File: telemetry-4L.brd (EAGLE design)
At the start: 69.8 x 22.9 mm, 64 parts, among them SW1 MF-SW-TACT-4.2MM, SW2 PCM12SMTR, U1 ATSAMD21G18A-MUT, U2 SPX3819M5-L-3-0, U3 MCP73831T-2ACI/OT, U4 IRLML6344TRPBF, U5 SIM868, U6 BMP280, U7 MPU-9250, X1 S2B-PH-SM4-TB(LF)(SN)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

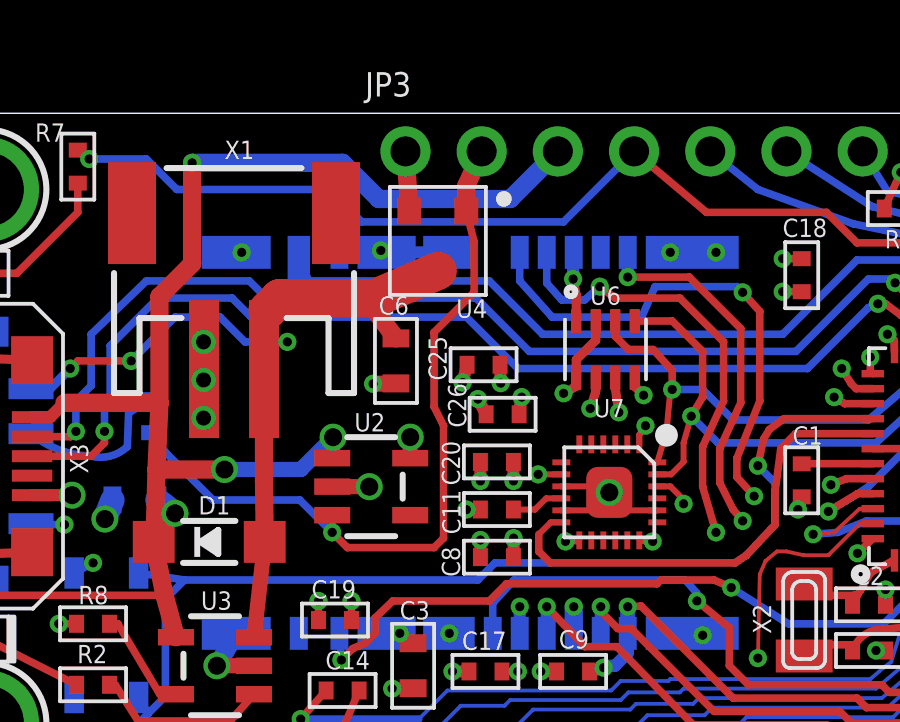
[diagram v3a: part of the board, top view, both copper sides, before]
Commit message: Swapped Power MOSFET Source and Drain so it's correct
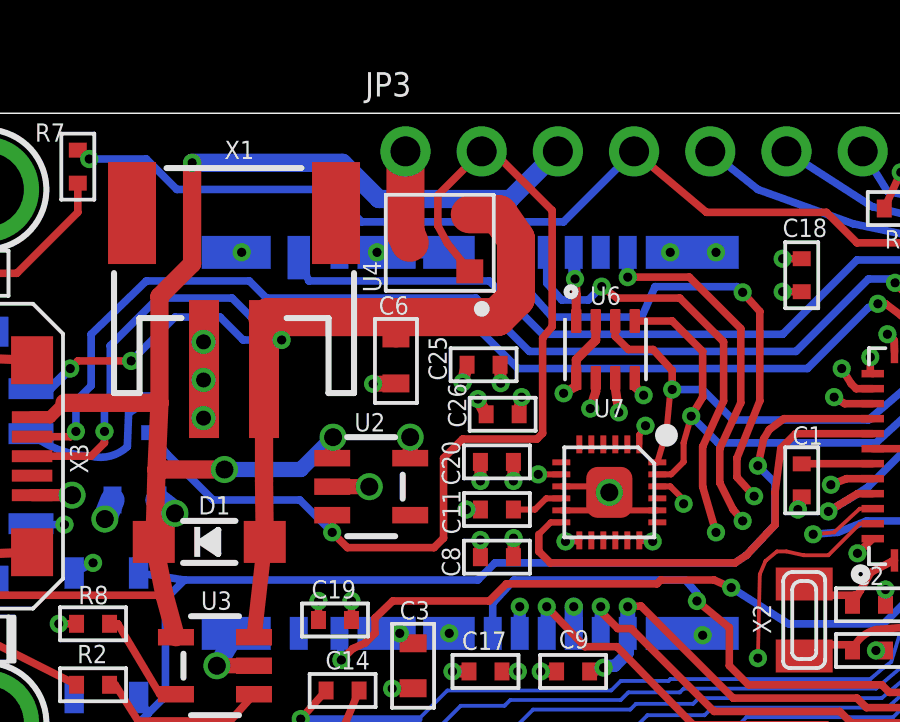
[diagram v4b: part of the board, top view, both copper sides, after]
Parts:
- moved U4 0.09 mm to (17.7, 18.5), turned to 180 degrees
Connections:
- net VBAT: now also U4.P$2; no longer U4.P$3
- net VBAT_ON: now also U4.P$3; no longer U4.P$2
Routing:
- net EN: track 25.8 -> 34.1 mm
- net VBAT: track 29.3 -> 34.4 mm
- net VBAT_ON: track 58.8 -> 59.9 mm

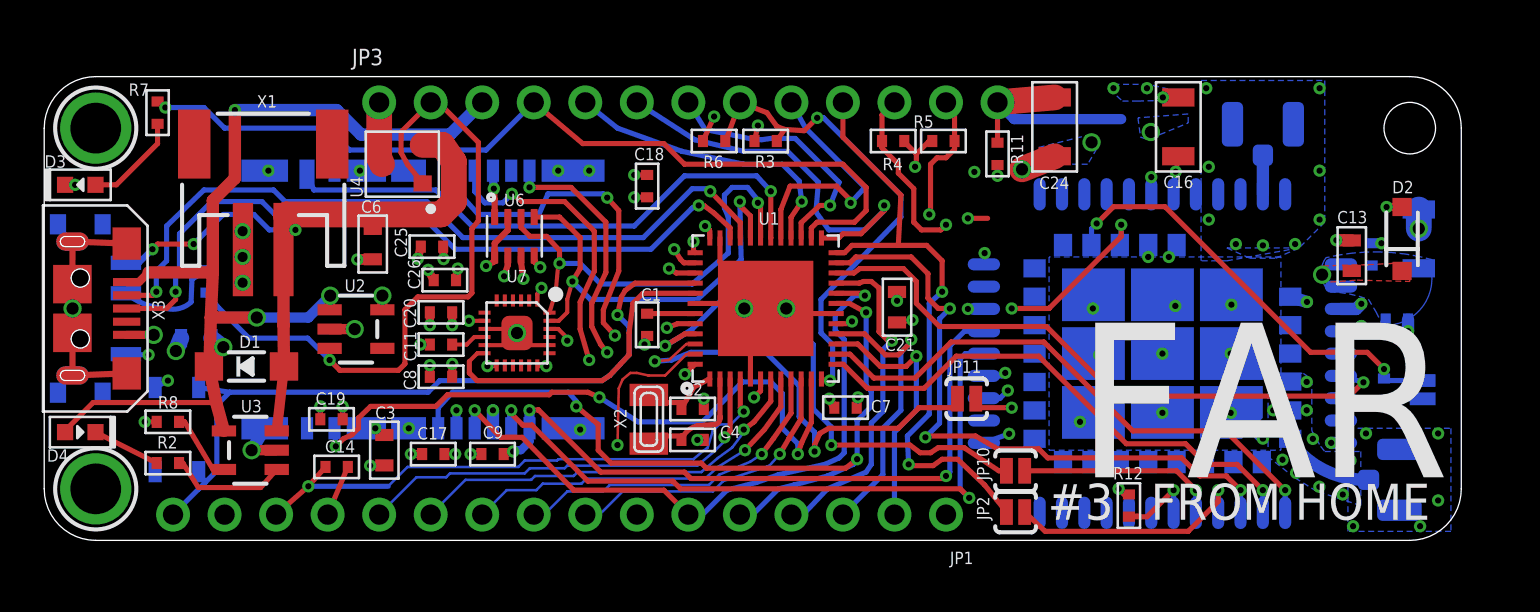
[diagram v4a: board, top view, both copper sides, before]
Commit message: Removed 5V power supply. This can be on shield!
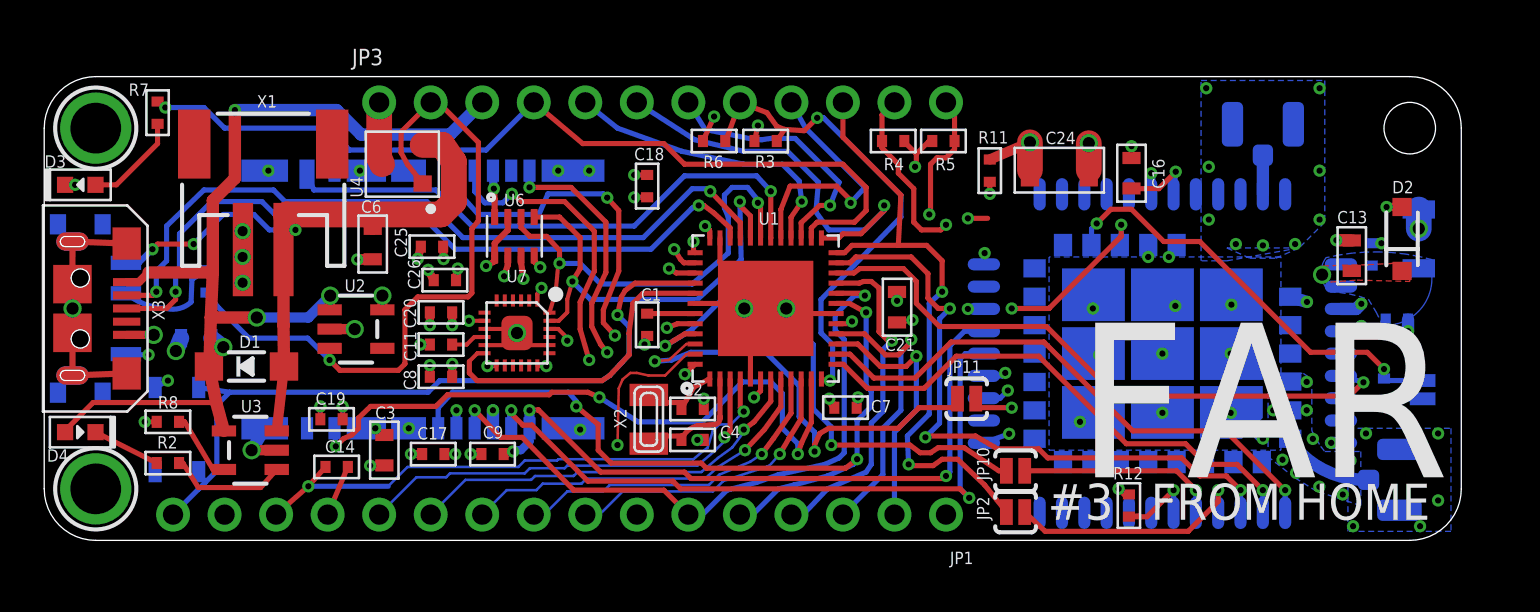
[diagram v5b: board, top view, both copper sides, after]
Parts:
- C16: value 100uF -> 10uF; device MF_Passives:C1206 -> MF_Passives:C0603
- JP3: device microbuilder:1X13_ROUND_70 -> microbuilder:1X12_ROUND
- moved C16 3.25 mm to (53.6, 18.1)
- moved C24 2.15 mm to (50.0, 18.2), turned to 0 degrees
- moved JP3 1.27 mm to (30.5, 21.6)
- moved R11 0.91 mm to (46.6, 18.2)
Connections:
- removed net 5.0V: C24.P$1, JP3.13, R11.P$1
- net VBAT_ON: now also C24.P$1, R11.P$1
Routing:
- net 5.0V: track 11.3 -> 0.00 mm
- net GND: track 117.1 -> 114.0 mm, vias 96 -> 94
- net VBAT_ON: track 59.9 -> 58.0 mm, vias 5 -> 3
- net N$29: track 1.89 -> 3.65 mm

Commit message: Ryddet litt i tracene
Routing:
- net AREF: track 28.3 -> 27.3 mm
- net SERVO_EN: track 18.2 -> 17.3 mm, vias 2 -> 1
- net D8/SD_CS: track 32.9 -> 31.9 mm
- net A1: track 20.3 -> 19.7 mm
- net A3: track 16.5 -> 16.0 mm
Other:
- board text added: "#4"
- board text removed: "#3"
- board text removed: "5V"

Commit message: Hooked GPS_1PPS to a normal pin, instead of SWDIO
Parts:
- removed JP11: JUMPER-PAD-2-NOYES_SILK, SparkFun-Passives:PAD-JUMPER-2-NO_YES_SILK
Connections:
- removed net SERVO_EN: U1.39
- net GPS_1PPS: now also U1.39; no longer JP11.2
- net SWDIO: no longer JP11.1
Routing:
- net GPS_1PPS: track 16.1 -> 35.7 mm, vias 3 -> 4
- net SERVO_EN: track 17.3 -> 0.00 mm, vias 1 -> 0
- net SWDIO: track 23.3 -> 7.97 mm, vias 2 -> 1
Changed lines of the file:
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@@
 <layers>
 <layer number="1" name="Top" color="4" fill="1" visible="yes" active="yes"/>
-<layer number="2" name="$GND" color="1" fill="3" visible="yes" active="yes"/>
+<layer number="2" name="$GND" color="1" fill="3" visible="no" active="yes"/>
 <layer number="3" name="Route3" color="4" fill="3" visible="no" active="no"/>
 <layer number="14" name="Route14" color="1" fill="6" visible="no" active="no"/>
@@
 <attribute name="VALUE" x="46.971" y="1.778" size="0.4064" layer="27"/>
 </element>
-<element name="JP11" library="SparkFun-Passives" package="PAD-JUMPER-2-NO_YES_SILK" value="JUMPER-PAD-2-NOYES_SILK" x="45.466" y="6.985" smashed="yes">
-<attribute name="POPULATE" value="0" x="45.466" y="6.985" size="1.778" layer="27" display="off"/>
-<attribute name="NAME" x="44.558" y="8.255" size="0.6096" layer="25" font="vector" ratio="18"/>
-<attribute name="VALUE" x="44.558" y="5.334" size="0.4064" layer="27"/>
-</element>
 <element name="JP3" library="microbuilder" package="1X12_ROUND" value="" x="30.48" y="21.59"/>
 <element name="SW1" library="MF_Switches" package="TACT4.2MM" value="MF-SW-TACT-4.2MM" x="6.5405" y="5.461" smashed="yes" rot="MR90">
@@
 <contactref element="TP2" pad="P$1"/>
 <wire x1="31.651" y1="9.68" x2="32.085" y2="9.68" width="0.127" layer="1"/>
-<contactref element="JP11" pad="1"/>
 <via x="30.099" y="8.8265" extent="1-16" drill="0.3048"/>
-<wire x1="31.877" y1="9.271" x2="35.56" y2="9.271" width="0.254" layer="16"/>
-<wire x1="35.56" y1="9.271" x2="37.211" y2="7.62" width="0.254" layer="16"/>
-<wire x1="37.211" y1="7.62" x2="37.211" y2="6.096" width="0.254" layer="16"/>
-<via x="37.973" y="4.3815" extent="1-16" drill="0.3048"/>
-<wire x1="37.211" y1="6.096" x2="37.973" y2="5.334" width="0.254" layer="16"/>
-<wire x1="37.973" y1="5.334" x2="37.973" y2="4.3815" width="0.254" layer="16"/>
-<wire x1="38.6715" y1="5.5245" x2="42.1005" y2="5.5245" width="0.254" layer="1"/>
-<wire x1="38.227" y1="5.2705" x2="38.6715" y2="5.5245" width="0.254" layer="1"/>
-<wire x1="42.1005" y1="5.5245" x2="43.1165" y2="6.5405" width="0.254" layer="1"/>
-<wire x1="43.1165" y1="6.5405" x2="44.831" y2="6.5405" width="0.254" layer="1"/>
-<wire x1="44.831" y1="6.5405" x2="44.958" y2="6.927" width="0.254" layer="1"/>
-<wire x1="44.958" y1="6.927" x2="45.016" y2="6.985" width="0.254" layer="1"/>
-<wire x1="37.973" y1="4.3815" x2="37.973" y2="4.699" width="0.254" layer="1"/>
-<wire x1="37.973" y1="4.699" x2="38.227" y2="5.2705" width="0.254" layer="1"/>
 <wire x1="31.651" y1="9.68" x2="30.7975" y2="8.89" width="0.127" layer="1"/>
 <wire x1="30.7975" y1="8.89" x2="30.099" y2="8.8265" width="0.127" layer="1"/>
-<wire x1="31.877" y1="9.271" x2="30.9245" y2="8.89" width="0.254" layer="16"/>
 <wire x1="30.9245" y1="8.89" x2="30.099" y2="8.8265" width="0.254" layer="16"/>
-<wire x1="35.56" y1="10.287" x2="35.56" y2="9.271" width="0.254" layer="16"/>
+<wire x1="35.56" y1="10.287" x2="30.9245" y2="8.89" width="0.254" layer="16"/>
 </signal>
 <signal name="N$5">
@@
 <wire x1="65.2145" y1="9.271" x2="62.4205" y2="9.271" width="0.254" layer="1"/>
 <wire x1="52.578" y1="16.3195" x2="53.594" y2="16.3195" width="0.254" layer="1"/>
-<wire x1="53.594" y1="16.3195" x2="55.1815" y2="14.732" width="0.254" layer="1"/>
-<wire x1="55.1815" y1="14.732" x2="56.9595" y2="14.732" width="0.254" layer="1"/>
+<wire x1="53.594" y1="16.3195" x2="56.9595" y2="14.732" width="0.254" layer="1"/>
 <wire x1="56.9595" y1="14.732" x2="62.4205" y2="9.271" width="0.254" layer="1"/>
 </signal>
@@
 <signal name="GPS_1PPS">
 <contactref element="U5" pad="60_"/>
-<contactref element="JP11" pad="2"/>
 <wire x1="53.018" y1="14.5575" x2="53.086" y2="14.6255" width="0.254" layer="16"/>
 <wire x1="53.086" y1="14.6255" x2="53.086" y2="15.5575" width="0.254" layer="16"/>
 <via x="53.086" y="15.5575" extent="1-16" drill="0.3048"/>
-<wire x1="53.086" y1="15.5575" x2="53.086" y2="14.986" width="0.254" layer="1"/>
-<wire x1="53.086" y1="14.986" x2="49.53" y2="11.43" width="0.254" layer="1"/>
-<wire x1="49.53" y1="11.43" x2="47.6885" y2="11.43" width="0.254" layer="1"/>
+<wire x1="53.086" y1="15.5575" x2="52.5145" y2="14.9225" width="0.254" layer="1"/>
+<wire x1="52.5145" y1="14.9225" x2="47.6885" y2="11.43" width="0.254" layer="1"/>
 <via x="47.6885" y="11.43" extent="1-16" drill="0.3048"/>
 <wire x1="47.6885" y1="11.43" x2="48.26" y2="10.8585" width="0.254" layer="2"/>
 <wire x1="48.26" y1="10.8585" x2="48.26" y2="7.112" width="0.254" layer="2"/>
 <wire x1="48.26" y1="7.112" x2="47.6885" y2="6.5405" width="0.254" layer="2"/>
-<via x="47.6885" y="6.5405" extent="1-16" drill="0.3048"/>
-<wire x1="47.6885" y1="6.5405" x2="45.9105" y2="6.5405" width="0.254" layer="1"/>
-<wire x1="45.9105" y1="6.5405" x2="45.9105" y2="6.985" width="0.254" layer="1"/>
-<wire x1="45.9105" y1="6.985" x2="45.916" y2="6.985" width="0.254" layer="1"/>
+<wire x1="47.6885" y1="6.5405" x2="47.6885" y2="6.5405" width="0" layer="19" extent="1-16"/>
+<wire x1="47.6885" y1="6.5405" x2="45.9105" y2="6.5405" width="0" layer="19" extent="1-16"/>
+<wire x1="45.9105" y1="6.5405" x2="45.9105" y2="6.985" width="0" layer="19" extent="1-16"/>
+<contactref element="U1" pad="39"/>
+<wire x1="32.085" y1="13.18" x2="31.1505" y2="13.18" width="0.254" layer="1"/>
+<wire x1="31.1505" y1="13.18" x2="30.7975" y2="13.3985" width="0.254" layer="1"/>
+<via x="30.7975" y="13.3985" extent="1-16" drill="0.3048"/>
+<wire x1="34.9885" y1="13.6525" x2="35.814" y2="14.478" width="0.254" layer="15"/>
+<wire x1="35.814" y1="14.478" x2="44.5135" y2="14.478" width="0.254" layer="15"/>
+<wire x1="30.7975" y1="13.3985" x2="31.5595" y2="13.6525" width="0.254" layer="15"/>
+<wire x1="31.5595" y1="13.6525" x2="34.9885" y2="13.6525" width="0.254" layer="15"/>
+<wire x1="44.5135" y1="14.478" x2="45.5295" y2="15.494" width="0.254" layer="15"/>
+<wire x1="47.6885" y1="11.43" x2="47.6885" y2="14.5415" width="0.254" layer="16"/>
+<wire x1="47.6885" y1="14.5415" x2="46.99" y2="15.24" width="0.254" layer="16"/>
+<wire x1="46.99" y1="15.24" x2="45.5295" y2="15.494" width="0.254" layer="16"/>
+<via x="45.5295" y="15.494" extent="1-16" drill="0.3048"/>
 </signal>
 <signal name="SIM_VDD">
@@
 <wire x1="46.609" y1="18.7745" x2="48.588" y2="19.6215" width="0.508" layer="1"/>
 </signal>
-<signal name="SERVO_EN">
-<contactref element="U1" pad="39"/>
-<wire x1="32.085" y1="13.18" x2="31.1505" y2="13.18" width="0.254" layer="1"/>
-<wire x1="31.1505" y1="13.18" x2="30.7975" y2="13.3985" width="0.254" layer="1"/>
-<via x="30.7975" y="13.3985" extent="1-16" drill="0.3048"/>
-<wire x1="34.9885" y1="13.6525" x2="35.814" y2="14.478" width="0.254" layer="15"/>
-<wire x1="35.814" y1="14.478" x2="44.5135" y2="14.478" width="0.254" layer="15"/>
-<wire x1="30.7975" y1="13.3985" x2="31.5595" y2="13.6525" width="0.254" layer="15"/>
-<wire x1="31.5595" y1="13.6525" x2="34.9885" y2="13.6525" width="0.254" layer="15"/>
-<wire x1="44.5135" y1="14.478" x2="45.5295" y2="15.494" width="0.254" layer="15"/>
-<wire x1="45.5295" y1="15.494" x2="45.5295" y2="15.875" width="0.254" layer="15"/>
-</signal>
 </signals>

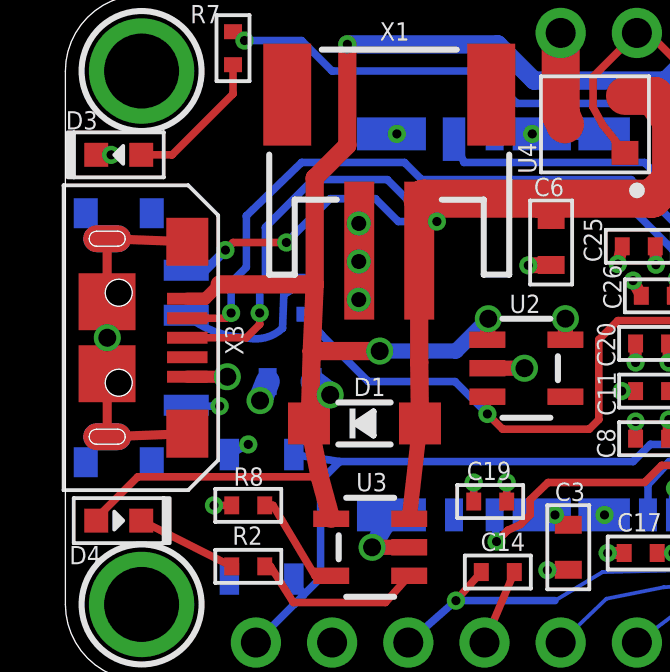
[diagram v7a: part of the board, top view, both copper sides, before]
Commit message: Updated libraries - short circuit in usb plug should be gone. Also moved USB and switch a tad to make it stick better
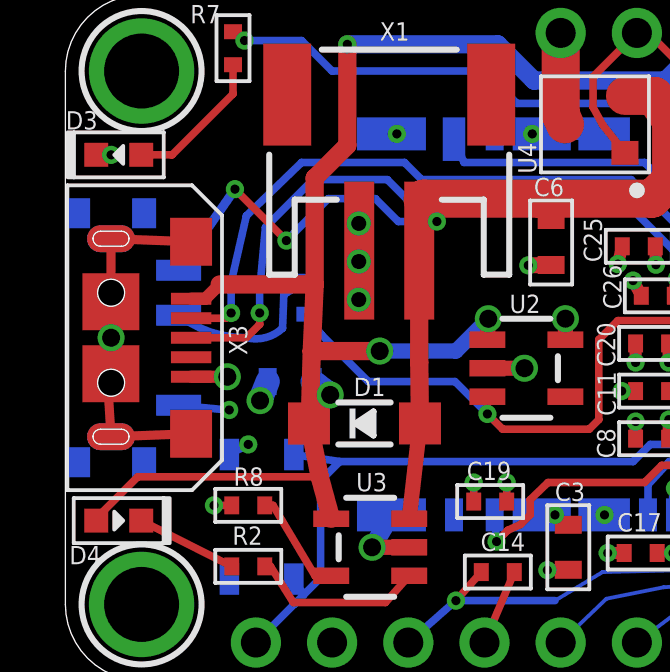
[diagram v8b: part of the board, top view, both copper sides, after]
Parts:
- moved SW2 0.25 mm to (1.52, 11.4)
- moved X3 0.13 mm to (2.92, 11.4)
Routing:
- net VBAT: track 34.4 -> 36.3 mm
- net GND: track 114.0 -> 114.8 mm
